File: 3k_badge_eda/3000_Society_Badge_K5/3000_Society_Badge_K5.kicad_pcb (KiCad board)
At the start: 2 copper layers, 195.2 x 165.9 mm, 25 parts, among them IC1 Trinket_M0

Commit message: 3d model updates
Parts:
- D10, D11, D12, D13, D21, D22, D41, D42: footprint 3000_Society_Badge:LED_D5.0mm-4_RGB_Wide_Pins -> 3000_Society_Badge:LED_D5.0mm-4_RGB

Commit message: Footprint and model cleanup
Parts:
- D10, D11, D12, D13, D21, D22, D41, D42: footprint 3000_Society_Badge:LED_D5.0mm-4_RGB -> 3000_Society_Badge:LED_D5.0mm-4_RGB_Neo
- D20, D40: footprint 3000_Society_Badge:LED_D8.0mm-4_RGB -> 3000_Society_Badge:LED_D8.0mm-4_RGB_Neo

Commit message: pcb work
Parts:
- moved R10 139.1 mm to (120.9, 90.8), turned to 90 degrees
- moved R02 129.9 mm to (114.2, 98.9), turned to 90 degrees
- moved R01 127.8 mm to (116.4, 98.2), turned to 90 degrees
- moved R04 114.2 mm to (143.1, 83.8), turned to 90 degrees
- moved R05 90.5 mm to (145.2, 83.7), turned to 90 degrees
- moved R03 90.2 mm to (141.0, 84.8), turned to 90 degrees
- moved R20 69.1 mm to (191.8, 91.4)
- moved C04 57.0 mm to (221.6, 96.5), turned to 180 degrees
- moved R40 55.2 mm to (184.9, 72.4), turned to 180 degrees
- moved C03 46.0 mm to (226.1, 101.7), turned to 180 degrees
- moved C05 43.9 mm to (216.5, 91.9), turned to 180 degrees
- moved C02 40.2 mm to (230.0, 107.4), turned to 180 degrees
- moved C01 12.8 mm to (231.8, 113.8), turned to 180 degrees
- moved D13 8.93 mm to (130.5, 85.5), turned to 335 degrees
- moved D12 8.43 mm to (137.5, 80.9), turned to 155 degrees
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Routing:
- net Net-(C01-Pad2): track 0.00 -> 259.3 mm
- net Net-(C02-Pad1): track 0.00 -> 180.4 mm
- net Net-(C01-Pad1): track 0.00 -> 174.2 mm
- net Net-(IC1-Pad10): track 0.00 -> 138.4 mm
- net Net-(C03-Pad1): track 0.00 -> 119.0 mm
- net Net-(C04-Pad1): track 0.00 -> 114.7 mm
- net Net-(C05-Pad1): track 0.00 -> 109.1 mm
- net Net-(IC1-Pad8): track 0.00 -> 74.2 mm
- net (no net): track 0.00 -> 42.7 mm
- net Net-(D10-Pad4): track 0.00 -> 12.9 mm
- net Net-(D21-Pad1): track 0.00 -> 11.2 mm
- net Net-(D41-Pad1): track 0.00 -> 9.28 mm
- net Net-(D20-Pad4): track 0.00 -> 9.25 mm
- net Net-(IC1-Pad3): track 0.00 -> 8.78 mm
- net Net-(D12-Pad1): track 0.00 -> 7.45 mm
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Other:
- outline, holes or cut-outs redrawn

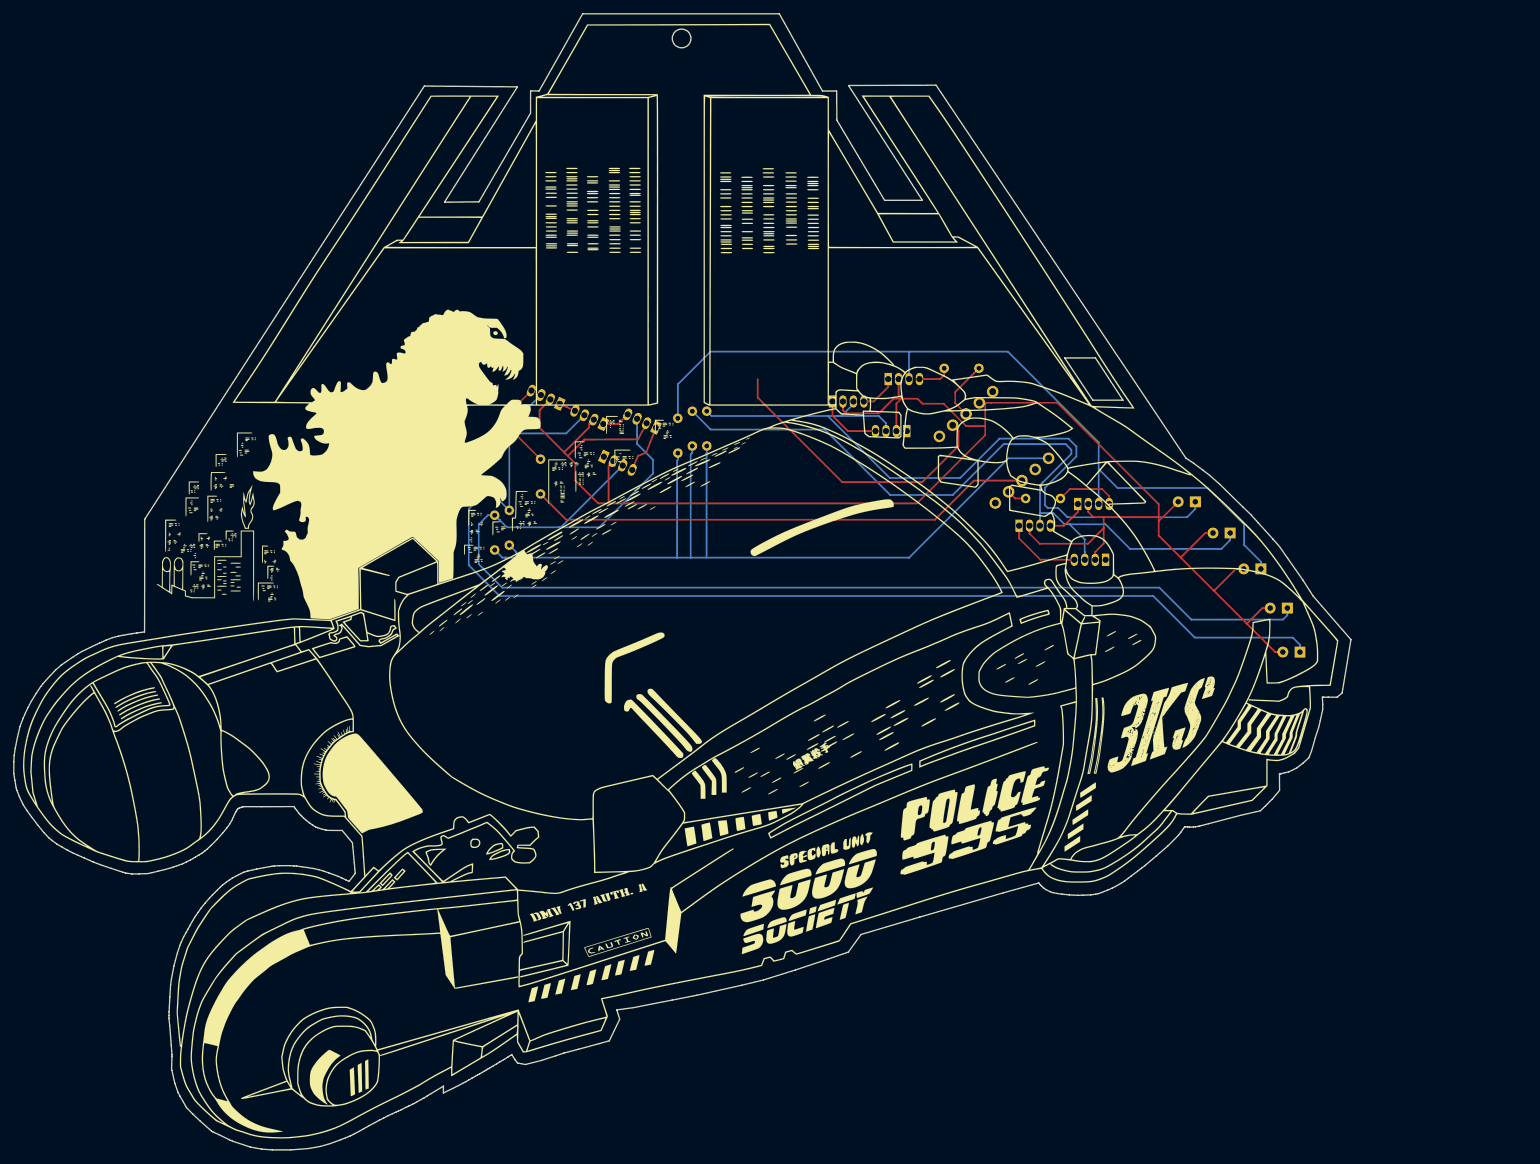
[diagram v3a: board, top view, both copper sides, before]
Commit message: Added Copper Touch Pad to PCB
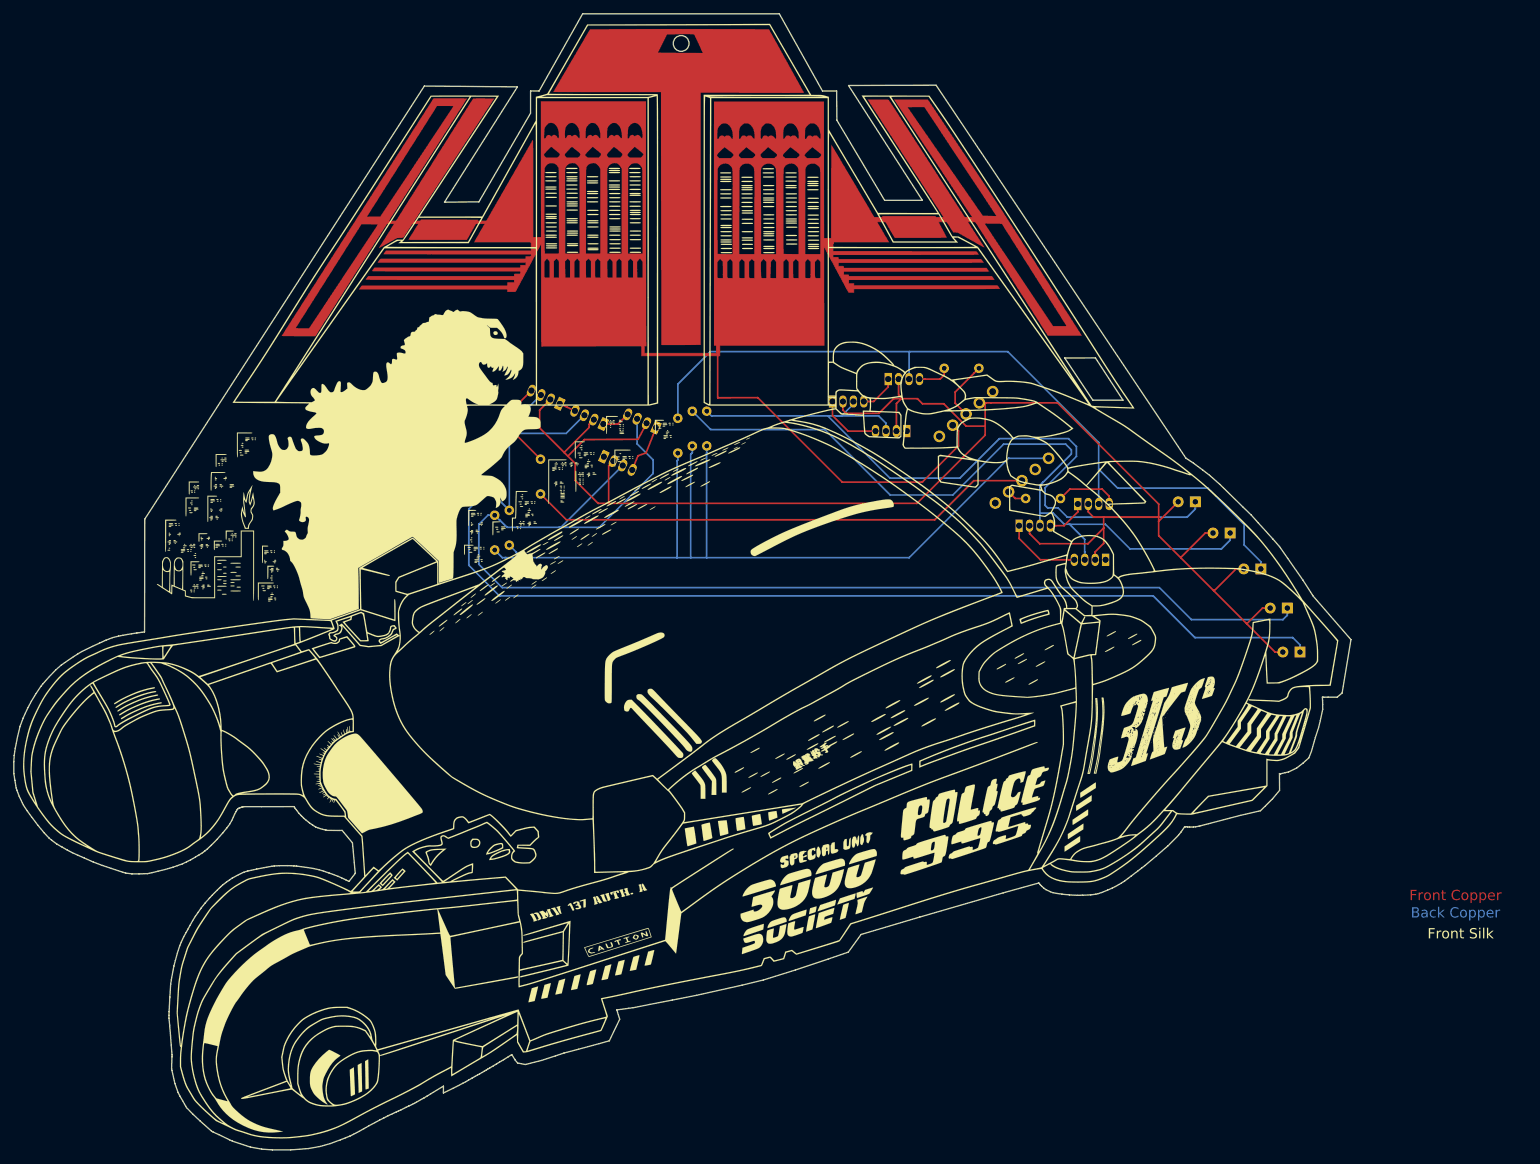
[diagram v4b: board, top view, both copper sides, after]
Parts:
- added TTP**: Tyrell_Touch_Pad, 3000_Society_Badge:Tyrell_Touch_Pad, F.Cu at (141.5, 46.1)
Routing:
- net (no net): track 42.7 -> 52.2 mm
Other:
- outline, holes or cut-outs redrawn
- board text added: "Back Copper"
- board text added: "Back Silk"
- board text added: "Back Solder Mask"
- board text added: "Front Copper"
- board text added: "Front Fab"
- board text added: "Front Silk"
- board text added: "Front Solder Mask"

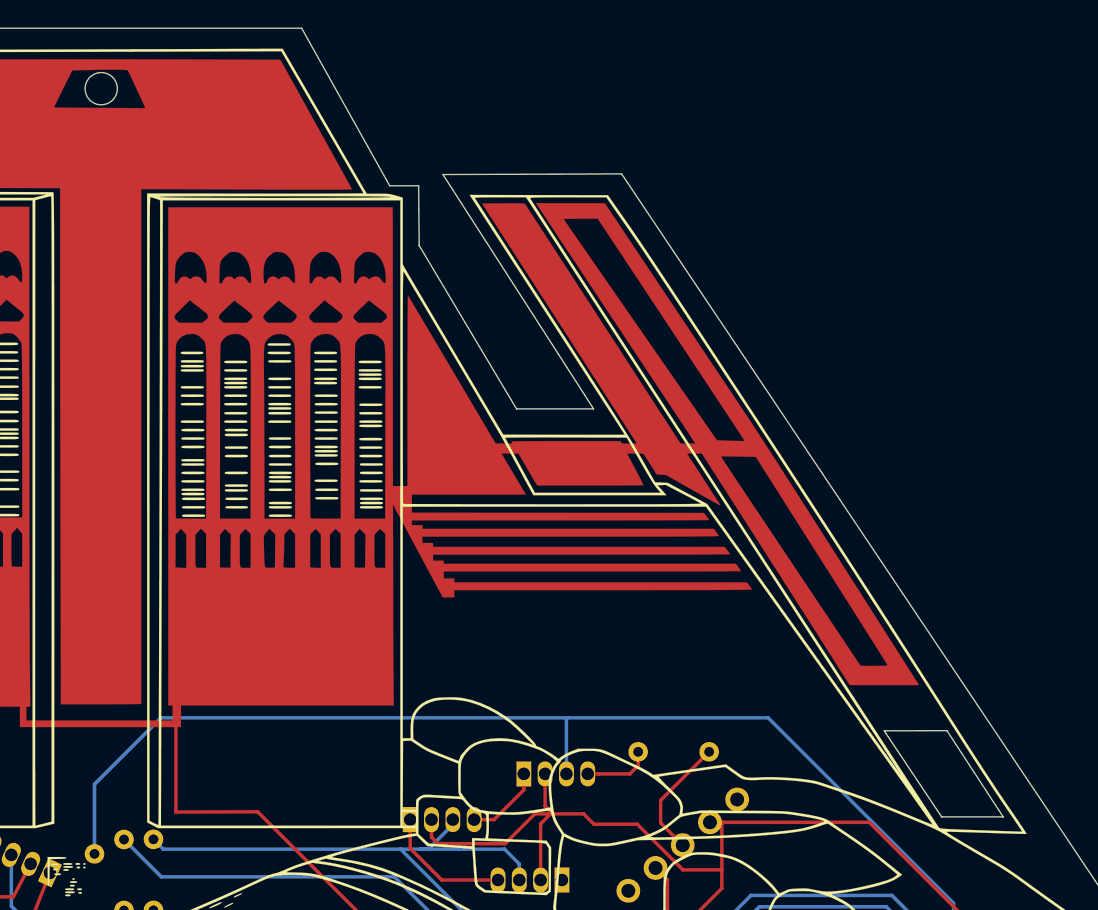
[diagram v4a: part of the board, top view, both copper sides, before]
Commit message: Back Silkscreen Work
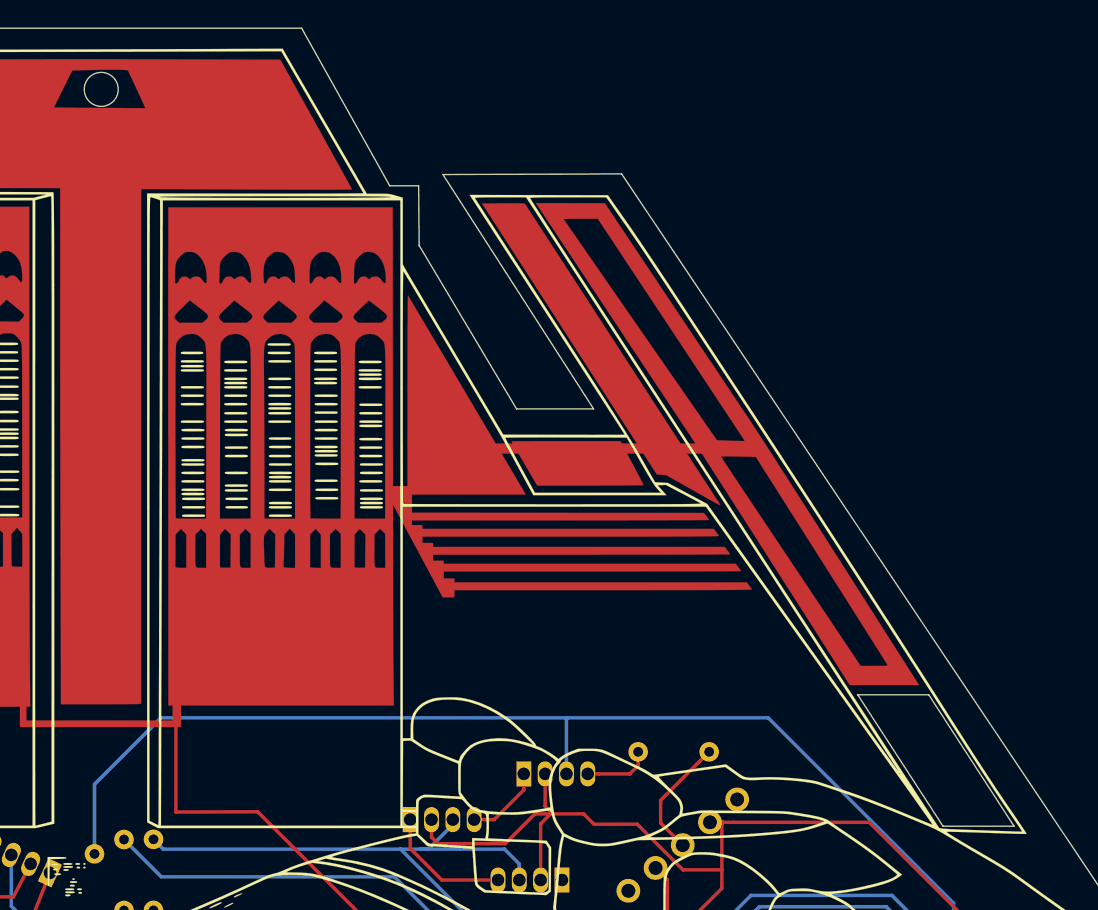
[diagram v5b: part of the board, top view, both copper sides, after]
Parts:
- added G***: 3000_Society_Logo_Back_Small, 3000_Society_Badge:3000_Society_Logo_Back_Small, F.Cu at (140.5, 51.1)
- added REF**: USB_Battery_Pack, 3000_Society_Badge:USB_Battery_Pack, F.Cu at (146.6, 126.5)
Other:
- outline, holes or cut-outs redrawn
- board text added: "Badge Design by @alt_bier https://github.com/gowenrw/3k_badge"
- board text added: "Godzilla vs. Blade Runner"
- board text added: "Presents"

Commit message: Board Layout Updates
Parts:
- removed TTP**: Tyrell_Touch_Pad, 3000_Society_Badge:Tyrell_Touch_Pad
- added TP1: TouchPad, 3000_Society_Badge:Tyrell_Touch_Pad, F.Cu at (141.5, 46.0)
- moved G*** 1.30 mm to (140.5, 49.8)
- moved REF** 0.59 mm to (146.2, 127.0)
- renumbered C01 to C1, C02 to C2, C03 to C3, C04 to C4, C05 to C5, R01 to R1, R02 to R2, R03 to R3, R04 to R4, R05 to R5
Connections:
- IC1 pad 4: (no net) -> Net-(IC1-Pad4)
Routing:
- net (no net): track 52.2 -> 0.00 mm
- net Net-(IC1-Pad4): track 0.00 -> 50.6 mm
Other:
- outline, holes or cut-outs redrawn
- board text added: "Badge Design by @alt_bier https://3kbadge.altbier.us/"
- board text removed: "Badge Design by @alt_bier https://github.com/gowenrw/3k_badge"
